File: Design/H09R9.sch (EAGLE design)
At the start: 24 parts, among them P1 HEXABIT_17.32, U1 STM32F091CBU6, U2 TSD305-1C55, X1 XTALL_CSTCE8M00G52

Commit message: -Standarize the files and folders
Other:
- note added: "H09R9"
- note added: "H09R9_Backend"
- note added: "H09R9_Frontend"
- note added: "Thermopile Module"
- note removed: "H09R9x"
- note removed: "H09R9x_Backend"
- note removed: "H09R9x_Frontend"
- note removed: "Hussein Jawish"
- note removed: "thermopile module"

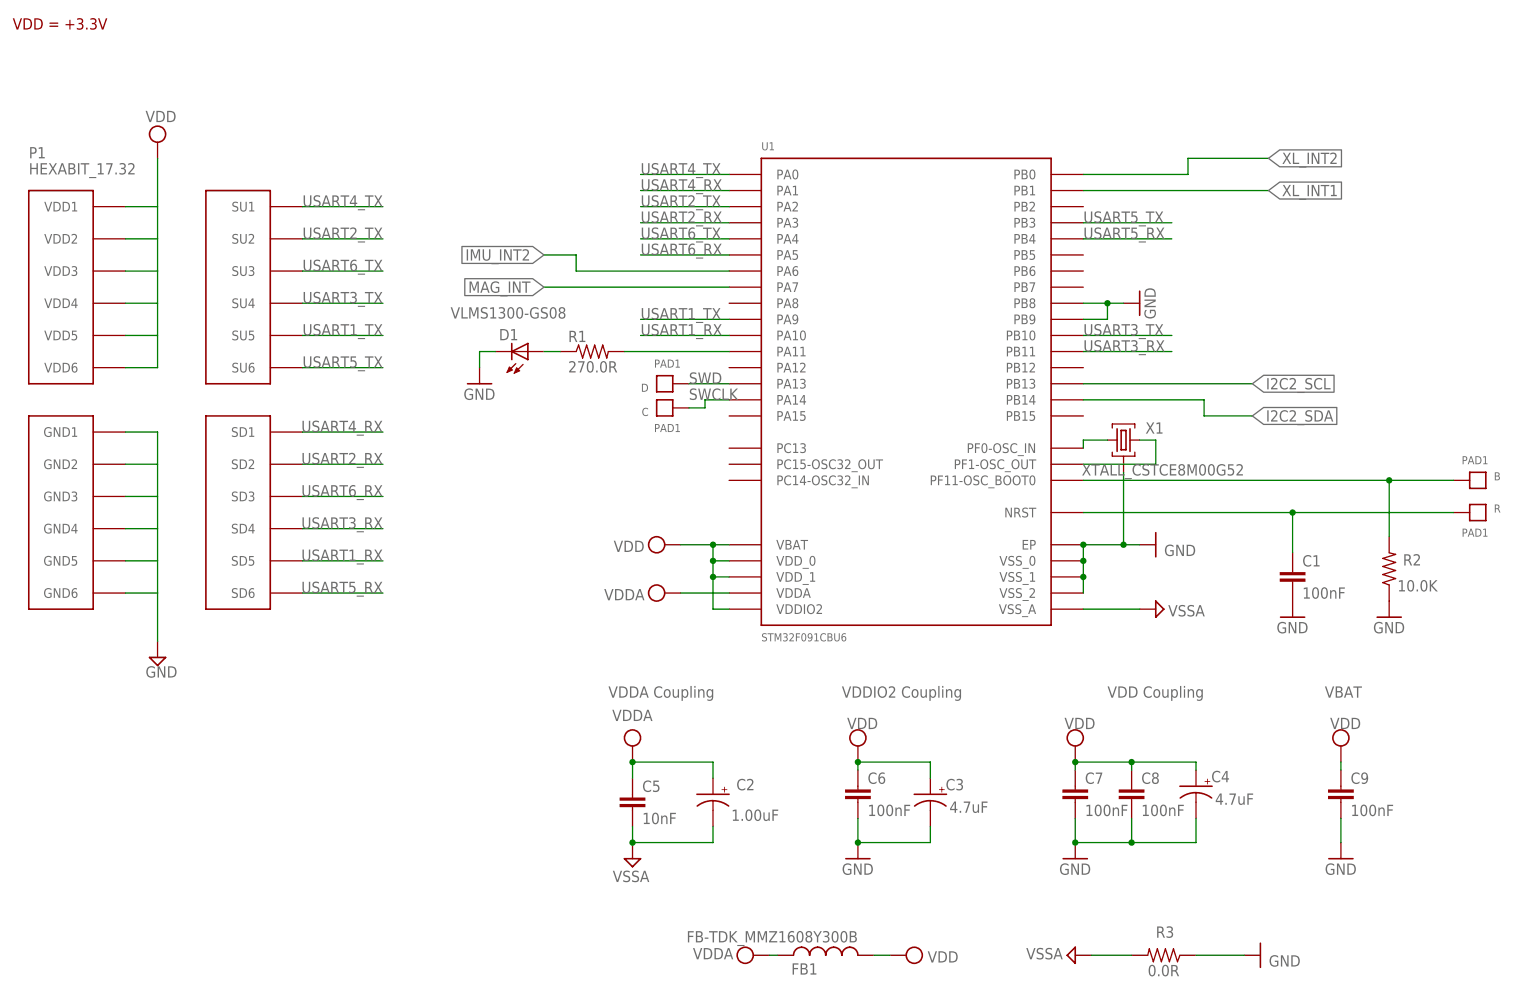
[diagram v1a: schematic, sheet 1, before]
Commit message: - The reviewed version is complete. - The upgraded version features the STM32G0B1CEU6N MCU. - Pull-up resistors have been added to the I2C Bus.
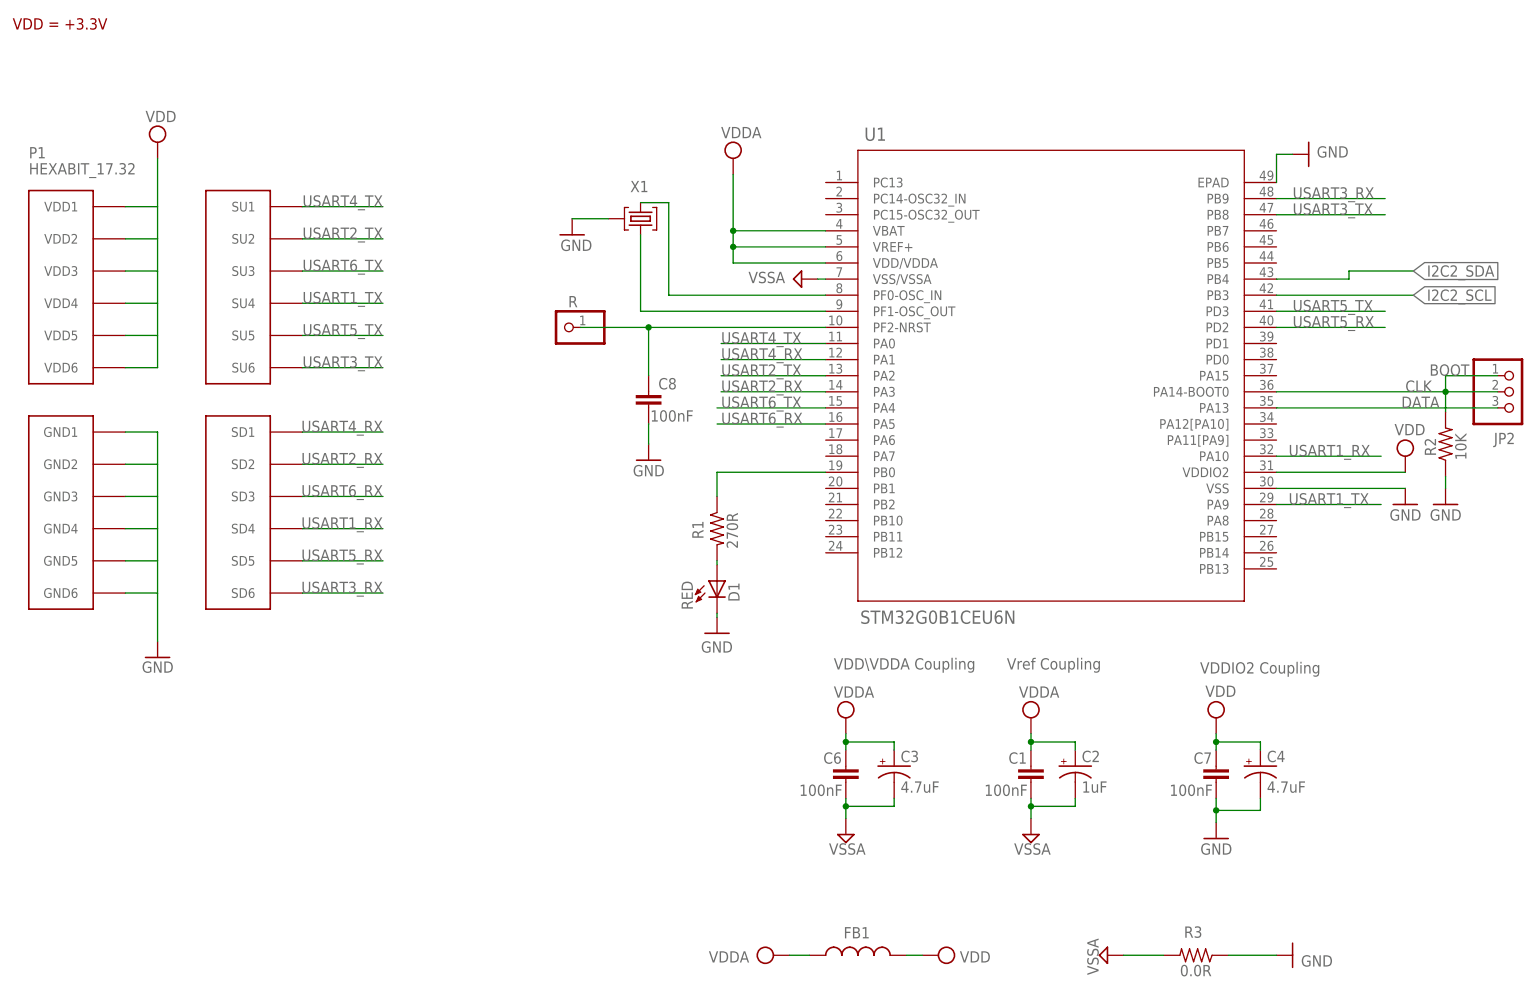
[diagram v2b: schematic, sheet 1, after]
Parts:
- removed B, C, D: PAD1, Hexabitz:PAD1
- removed C5: 10nF, Hexabitz:C-0603
- removed C9: 100nF, Hexabitz:C-0603
- added JP2: (no value), pinhead:PINHD-1X3
- added R4, R5: 10K, HEXABITZ_RCLS:R-0603
- C1, C6, C7, C8: device Hexabitz:C-0603 -> HEXABITZ_RCLS:C-0603; CAPACITANCE 100nF -> (none); MFN AVX -> (none); MPN 0603YC104K4T2A -> (none); OCTOPART_URL https://octopart.com/0603yc104k4t2a-avx+interconnect+%2F+el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 -> (none); TOLERANCE 10% -> (none); VOLTAGE_RATING 16.0 V -> (none)
- C10: device Hexabitz:C-0603 -> HEXABITZ_RCLS:C-0603
- C11: device Hexabitz:C-0805-POL -> HEXABITZ_RCLS:C-0805-POL
- C2: value 1.00uF -> 1uF; device Hexabitz:C-0805-POL -> HEXABITZ_RCLS:C-0805-POL; CAPACITANCE 1.00uF -> (none); MFN AVX -> (none); MPN TAJR105M016RNJ -> (none); OCTOPART_URL http://octopart.com/tajr105m016rnj-avx-1188552 -> (none); TOLERANCE 10% -> (none); VOLTAGE_RATING 16.0 V -> (none)
- C3: device Hexabitz:C-0805-POL -> HEXABITZ_RCLS:C-0805-POL; CAPACITANCE 4.7uF -> (none); MFN Panasonic -> (none); MPN 10TPU4R7MSI -> (none); OCTOPART_URL https://octopart.com/10tpu4r7msi-panasonic-29487748 -> (none); TOLERANCE 20% -> (none); VOLTAGE_RATING 10.0 V -> (none)
- C4: device Hexabitz:C-0805-POL -> HEXABITZ_RCLS:C-0805-POL; CAPACITANCE 4.7uF -> (none); MFN Panasonic -> (none); MPN 10TPU4R7MSI -> (none); OCTOPART_URL https://octopart.com/10tpu4r7msi-panasonic-29487748 -> (none); TOLERANCE 10% -> (none); VOLTAGE_RATING 10 V -> (none)
- D1: value VLMS1300-GS08 -> RED; device Hexabitz:VLMS1300-GS08 -> HEXABITZ_USER_INTERFACE_PARTS:VLMS1300-GS08
- FB1: device Hexabitz:FB-TDK_MMZ1608Y300B -> HEXABITZ_RCLS:FB-TDK_MMZ1608Y300B
- P1: device Hexabitz:HEXABIT_17.32 -> hexabitz_connectors:HEXABIT_17.32
- R: value PAD1 -> R; device Hexabitz:PAD1 -> HEXABITZ_USER_INTERFACE_PARTS:PINHD-1X1
- R1: value 270.0R -> 270R; device Hexabitz:R-0603 -> HEXABITZ_RCLS:R-0603; MFN Panasonic -> (none); MPN ERJ-3GEYJ271V -> (none); OCTOPART_URL https://octopart.com/erj-3geyj271v-panasonic-55560546 -> (none); RESISTANCE 270.0 Ohm -> (none); TOLERANCE 5% -> (none)
- R2: value 10.0K -> 10K; device Hexabitz:R-0603 -> HEXABITZ_RCLS:R-0603; MFN Vishay -> (none); MPN CRCW060310K0JNEB -> (none); OCTOPART_URL https://octopart.com/crcw060310k0jneb-vishay-46603269 -> (none); RESISTANCE 10.0K Ohm -> (none); TOLERANCE 5% -> (none)
- R3: device Hexabitz:R-0603 -> HEXABITZ_RCLS:R-0603; MFN Vishay -> Yageo; MPN CRCW06030000Z0EAHP -> RC0603JR-070RL; OCTOPART_URL https://octopart.com/crcw06030000z0eahp-vishay-44320230 -> https://octopart.com/rc0603jr-070rl-yageo-1241539?r=sp&s=X2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
- U1: value STM32F091CBU6 -> STM32G0B1CEU6N; device Hexabitz:STM32F091CBU6 -> HEXABITZ_ICs:STM32G0B1CEU6N
- X1: device Hexabitz:XTALL_CSTCE8M00G52 -> HEXABITZ_RCLS:XTALL_CSTCE8M00G52
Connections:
- removed net B1: B.P$1, R2.2, U1.PF11-OSC_BOOT0
- removed net IMU_INT2: U1.PA6
- removed net MAG_INT: U1.PA7
- removed net R1: C1.1, R.P$1, U1.NRST
- removed net SWCLK: C.P$1, U1.PA14
- removed net SWD: D.P$1, U1.PA13
- removed net XL_INT1: U1.PB1
- removed net XL_INT2: U1.PB0
- new net CLK: JP2.1, JP2.2, R2.2, U1.PA14-BOOT0
- new net DATA: JP2.3, U1.PA13
- new net N$1: R1.1, U1.PB0
- net GND: now also U1.EPAD, U1.VSS; no longer C1.2, C3.-, C6.2, C9.2, U1.EP, U1.PB8, U1.PB9, U1.VSS_0, U1.VSS_1, U1.VSS_2
- net I2C2_SCL: now also R4.1, U1.PB3; no longer U1.PB13
- net I2C2_SDA: now also R5.1, U1.PB4; no longer U1.PB14
- net N$3: now also D1.A; no longer U1.PA11
- net N$4: now also C8.1, R.1, U1.PF2-NRST; no longer D1.A, R1.1
- net N$5: now also U1.PF1-OSC_OUT; no longer U1.PF0-OSC_IN
- net N$6: now also U1.PF0-OSC_IN; no longer U1.PF1-OSC_OUT
- net USART1_RX: now also P1.SD4; no longer P1.SD5
- net USART1_TX: now also P1.SU4; no longer P1.SU5
- net USART3_RX: now also P1.SD6, U1.PB9; no longer P1.SD4, U1.PB11
- net USART3_TX: now also P1.SU6, U1.PB8; no longer P1.SU4, U1.PB10
- net USART5_RX: now also P1.SD5, U1.PD2; no longer P1.SD6, U1.PB4
- net USART5_TX: now also P1.SU5, U1.PD3; no longer P1.SU6, U1.PB3
- net VDD: now also R4.2, R5.2; no longer C3.+, C6.1, C8.1, C9.1, U1.VBAT, U1.VDD_0, U1.VDD_1
- net VDDA: now also C1.1, C3.+, C6.1, U1.VBAT, U1.VDD/VDDA, U1.VREF+; no longer C5.1, U1.VDDA
- net VSSA: now also C1.2, C3.-, C6.2, U1.VSS/VSSA; no longer C5.2, U1.VSS_A
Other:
- note added: "BOOT"
- note added: "Thermopile Sensor Module"
- note added: "VDD\VDDA Coupling"
- note added: "Vref Coupling"
- note removed: "0"
- note removed: "Thermopile Module"
- note removed: "VBAT"
- note removed: "VDD Coupling"
- note removed: "VDDA Coupling"
- moved on the sheet: C1, C10, C11, C2, C3, C4, C6, C7, C8, D1, FB1, R1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
